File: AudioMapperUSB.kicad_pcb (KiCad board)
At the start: 2 copper layers, 100 x 100 mm, 152 parts, among them J1 USB_B, J10 Conn_01x01, J11 Conn_01x01, J12 Conn_Coaxial, J13 Conn_Coaxial, J14 Conn_Coaxial, J15 Conn_Coaxial, J16 Audio-Jack-2, J17 Audio-Jack-2, J18 Audio-Jack-2, J19 Audio-Jack-2, J2 Audio-Jack-2, J20 Audio-Jack-2, J21 Audio-Jack-2, J3 Conn_01x02, J4 Audio-Jack-2, J5 Conn_01x02, J6 Conn_01x02, J7 Conn_01x02, J8 Conn_01x01, J9 Conn_01x01, Q1 SS8550, Q2 MMBT3904, Q3 MMBT3904, U1 AMS1117-3.3, U2 PCM2900, U3 OPA2170, U4 OPA2170, U5 OPA2170, U6 OPA2170, Y1 12 MHz

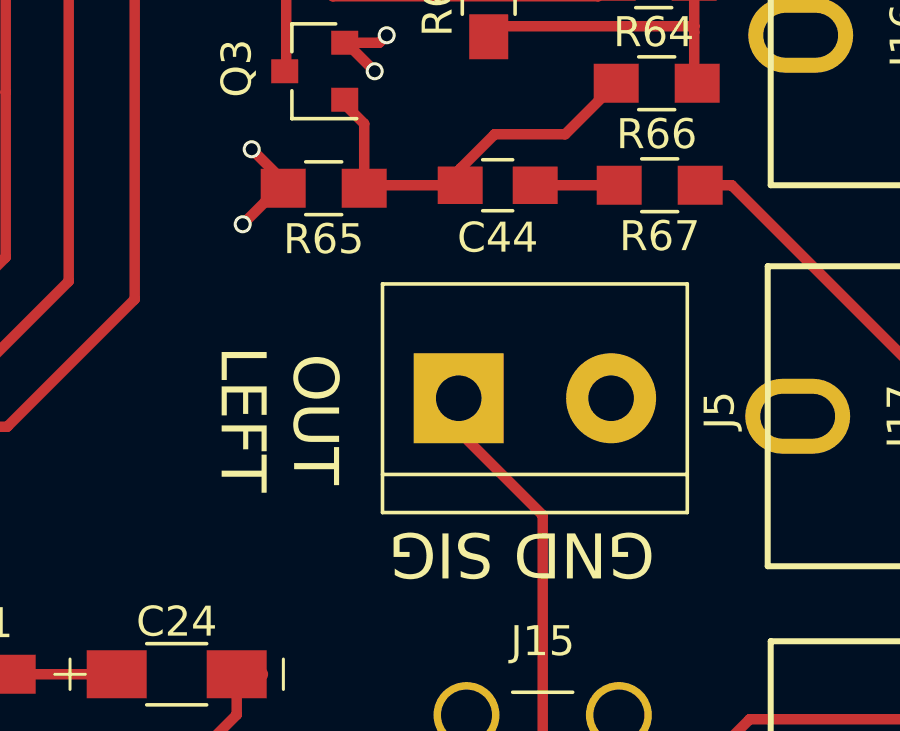
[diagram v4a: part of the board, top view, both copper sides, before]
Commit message: Added pulldown resistor to input
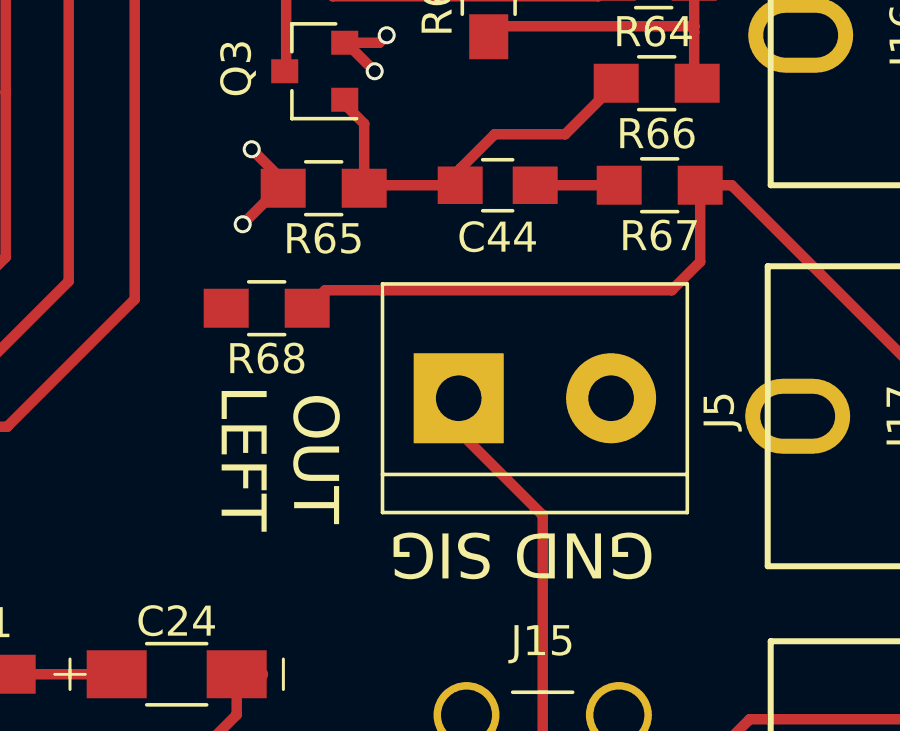
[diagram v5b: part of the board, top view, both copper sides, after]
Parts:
- added R68: 100R, Resistors_SMD:R_0805_HandSoldering, F.Cu at (100.1, 87.2)
- R67: value 100R -> 220R
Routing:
- net Net-(J17-Pad1): track 11.7 -> 28.0 mm
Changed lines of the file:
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@@
 (kicad_pcb (version 4) (host pcbnew 4.0.7)
   (general
-    (links 304)
+    (links 306)
     (no_connects 0)
     (area 28.252381 22.024999 131.74762 131.200001)
     (thickness 1.6)
     (drawings 36)
-    (tracks 1181)
+    (tracks 1185)
     (zones 0)
-    (modules 152)
+    (modules 153)
     (nets 65)
   )
@@
       (effects (font (size 1 1) (thickness 0.15)))
     )
-    (fp_text value 100R (at 0 1.75 180) (layer F.Fab)
+    (fp_text value 220R (at 0 1.75 180) (layer F.Fab)
       (effects (font (size 1 1) (thickness 0.15)))
     )
@@
     )
   )
+  (module Resistors_SMD:R_0805_HandSoldering (layer F.Cu)
+    (at 100.1 87.2 180)
+    (descr "Resistor SMD 0805, hand soldering")
+    (tags "resistor 0805")
+    (attr smd)
+    (fp_text reference R68 (at 0 -1.7 180) (layer F.SilkS)
+      (effects (font (size 1 1) (thickness 0.15)))
+    )
+    (fp_text value 100R (at 0 1.75 180) (layer F.Fab)
+      (effects (font (size 1 1) (thickness 0.15)))
+    )
+    (fp_text user %R (at 0 0 180) (layer F.Fab)
+      (effects (font (size 0.5 0.5) (thickness 0.075)))
+    )
+    (fp_line (start -1 0.62) (end -1 -0.62) (layer F.Fab) (width 0.1))
+    (fp_line (start 1 0.62) (end -1 0.62) (layer F.Fab) (width 0.1))
+    (fp_line (start 1 -0.62) (end 1 0.62) (layer F.Fab) (width 0.1))
+    (fp_line (start -1 -0.62) (end 1 -0.62) (layer F.Fab) (width 0.1))
+    (fp_line (start 0.6 0.88) (end -0.6 0.88) (layer F.SilkS) (width 0.12))
+    (fp_line (start -0.6 -0.88) (end 0.6 -0.88) (layer F.SilkS) (width 0.12))
+    (fp_line (start -2.35 -0.9) (end 2.35 -0.9) (layer F.CrtYd) (width 0.05))
+    (fp_line (start -2.35 -0.9) (end -2.35 0.9) (layer F.CrtYd) (width 0.05))
+    (fp_line (start 2.35 0.9) (end 2.35 -0.9) (layer F.CrtYd) (width 0.05))
+    (fp_line (start 2.35 0.9) (end -2.35 0.9) (layer F.CrtYd) (width 0.05))
+    (pad 1 smd rect (at -1.35 0 180) (size 1.5 1.3) (layers F.Cu F.Paste F.Mask)
+      (net 50 "Net-(J17-Pad1)"))
+    (pad 2 smd rect (at 1.35 0 180) (size 1.5 1.3) (layers F.Cu F.Paste F.Mask)
+      (net 2 GND))
+    (model ${KISYS3DMOD}/Resistors_SMD.3dshapes/R_0805.wrl
+      (at (xyz 0 0 0))
+      (scale (xyz 1 1 1))
+      (rotate (xyz 0 0 0))
+    )
+  )
   (gr_text "CHAIN IN" (at 31 106.6 270) (layer F.SilkS)
     (effects (font (size 1 1) (thickness 0.15)))
@@
     (effects (font (size 1 1) (thickness 0.15)))
   )
-  (gr_text "OUT\nLEFT" (at 100.5 90.9 270) (layer F.SilkS)
+  (gr_text "OUT\nLEFT" (at 100.5 92.2 270) (layer F.SilkS)
     (effects (font (size 1.5 1.5) (thickness 0.3)))
   )
@@
   (segment (start 127.1 67.9) (end 124.65 70.35) (width 0.35) (layer F.Cu) (net 49))
   (segment (start 124.65 70.35) (end 123.4 70.35) (width 0.35) (layer F.Cu) (net 49))
+  (segment (start 114.55 83.1) (end 114.55 85.65) (width 0.35) (layer F.Cu) (net 50))
+  (segment (start 113.6 86.6) (end 102.05 86.6) (width 0.35) (layer F.Cu) (net 50))
+  (segment (start 114.55 85.65) (end 113.6 86.6) (width 0.35) (layer F.Cu) (net 50))
+  (segment (start 102.05 86.6) (end 101.45 87.2) (width 0.35) (layer F.Cu) (net 50))
   (segment (start 122.8 90.8) (end 122.8 90.3) (width 0.35) (layer F.Cu) (net 50))
   (segment (start 122.8 90.3) (end 115.6 83.1) (width 0.35) (layer F.Cu) (net 50))

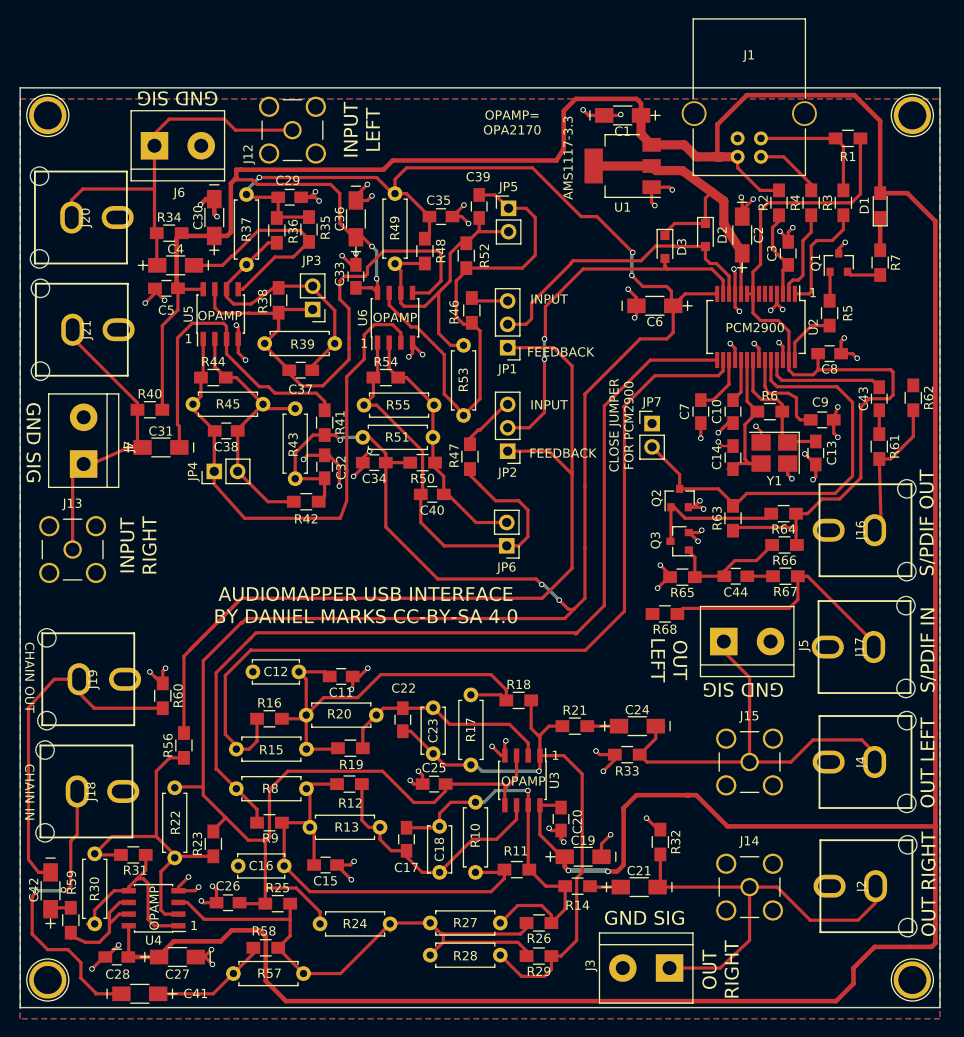
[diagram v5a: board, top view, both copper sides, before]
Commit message: Fixed backward polarity audio connectors.  Duh.
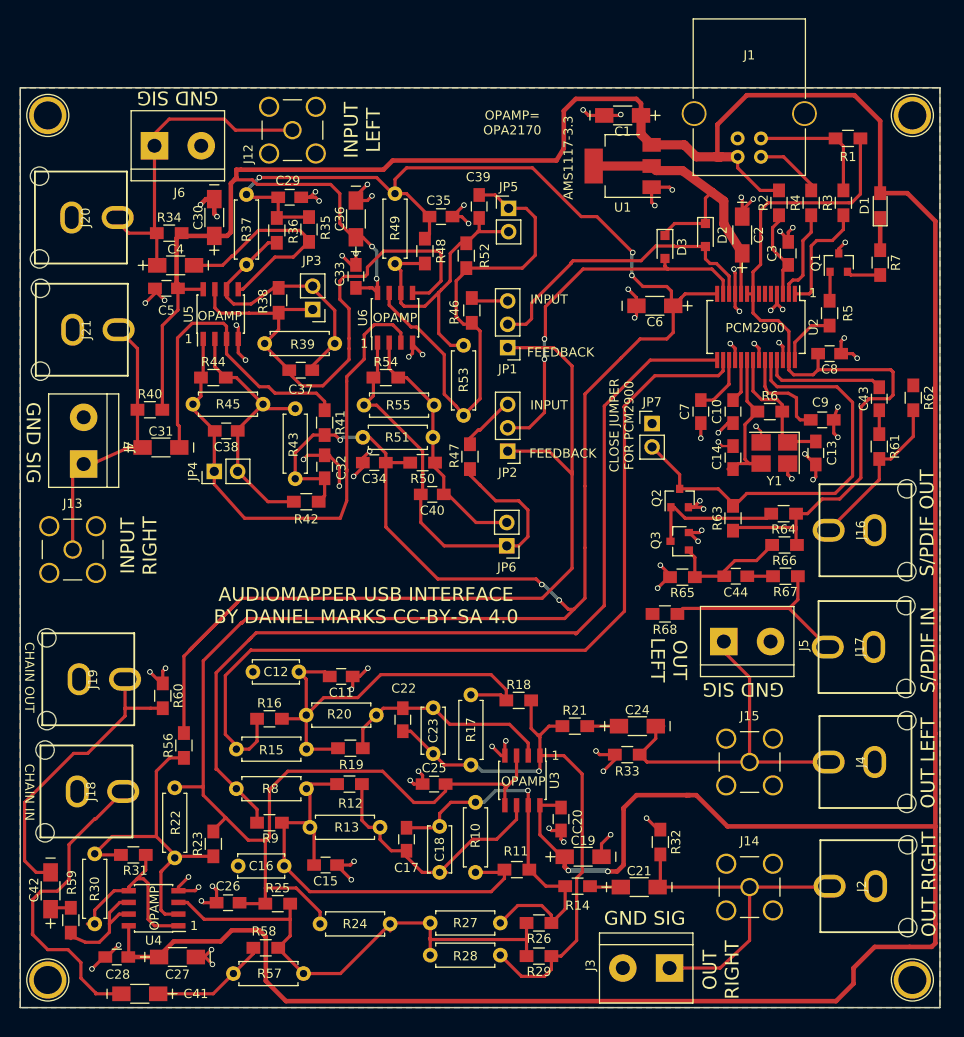
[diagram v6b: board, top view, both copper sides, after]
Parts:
- R63, R64: value 10k -> 1k
- R65: value 2k2 -> 10k
- R66: value 10k -> 100k
- R67: value 220R -> 100R
- R68: value 100R -> NC
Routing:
- net Net-(C21-Pad2): track 47.7 -> 38.7 mm
- net Net-(C24-Pad2): track 47.3 -> 39.8 mm
- net GND: track 154.9 -> 161.5 mm
- net Net-(C4-Pad1): track 42.9 -> 36.8 mm
- net Net-(R24-Pad2): track 64.0 -> 58.2 mm
- net Net-(J17-Pad1): track 28.0 -> 22.2 mm
- net Net-(C42-Pad2): track 39.4 -> 34.2 mm
- net Net-(C31-Pad1): track 32.7 -> 30.7 mm
- net Net-(J16-Pad1): track 15.6 -> 17.6 mm
- net Net-(C41-Pad2): track 33.8 -> 34.2 mm, vias 2 -> 0

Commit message: Added external power
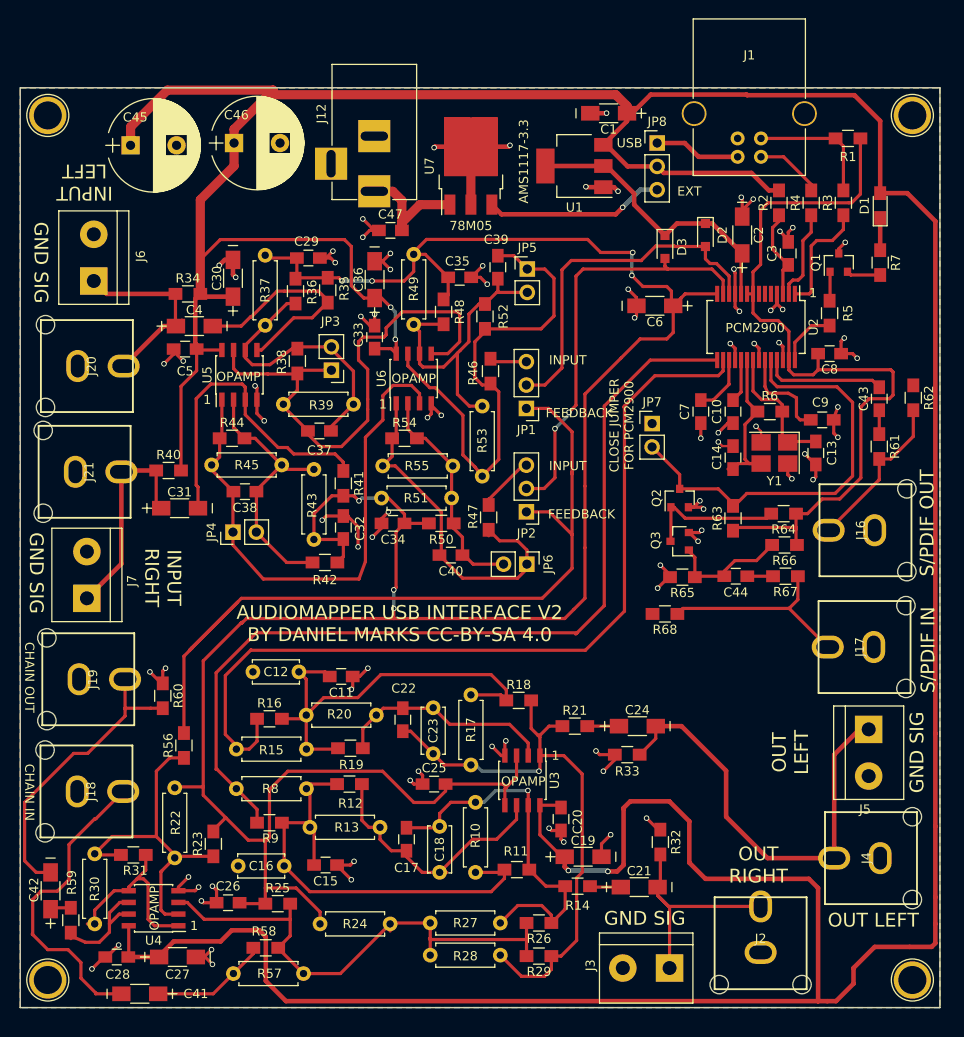
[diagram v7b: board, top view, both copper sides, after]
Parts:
- removed J13, J14, J15: Conn_Coaxial, Connectors:SMA_THT_Jack_Straight
- added C45: 1000 uF, Capacitors_THT:CP_Radial_D10.0mm_P5.00mm, F.Cu at (42.0, 36.2)
- added C46: 1000 uF, Capacitors_THT:CP_Radial_D10.0mm_P5.00mm, F.Cu at (53.2, 36.0)
- added C47: 1 uF, Capacitors_SMD:C_0805_HandSoldering, F.Cu at (70.2, 45.5)
- added JP8: Jumper_NC_Dual, Pin_Headers:Pin_Header_Straight_1x03_Pitch2.54mm, F.Cu at (99.2, 36.0)
- added U7: KA78M05_TO252, TO_SOT_Packages_SMD:TO-252-3_TabPin2, F.Cu at (79.0, 38.5)
- J12: value Conn_Coaxial -> Jack-DC; footprint Connectors:SMA_THT_Jack_Straight -> Connectors:BARREL_JACK
- moved J5 18.4 mm to (122.2, 99.8), turned to 270 degrees
- moved J20 16.2 mm to (37.2, 60.2)
- moved J6 16.1 mm to (38.0, 51.0), turned to 90 degrees
- moved J21 15.5 mm to (37.0, 71.8)
- moved J7 14.6 mm to (37.2, 85.5)
- moved J2 13.1 mm to (110.5, 123.0), turned to 180 degrees
- moved J12 11.1 mm to (68.5, 41.2), turned to 270 degrees
- moved J4 10.5 mm to (122.5, 113.8)
- moved C4 6.91 mm to (48.9, 55.9)
- moved C5 6.91 mm to (47.9, 58.4)
- moved R34 6.91 mm to (48.2, 52.4)
- moved JP5 6.91 mm to (85.1, 49.7)
- moved R46 6.91 mm to (81.1, 60.8)
- moved C29 6.91 mm to (61.3, 48.5)
- moved C31 6.91 mm to (47.3, 75.7)
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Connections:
- J1 pad 1: Net-(C1-Pad1) -> Net-(J1-Pad1)
- J12 pad 1: Net-(C4-Pad1) -> Net-(C47-Pad2)
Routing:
- net Net-(C1-Pad1): track 416.8 -> 466.7 mm
- net VCOM: track 308.3 -> 275.6 mm, vias 6 -> 7
- net Net-(JP8-Pad3): track 0.00 -> 19.5 mm, vias 0 -> 1
- net Net-(C4-Pad1): track 36.8 -> 21.7 mm
- net Net-(C47-Pad2): track 0.00 -> 13.5 mm
- net Net-(C21-Pad2): track 38.7 -> 25.3 mm
- net GND: track 161.5 -> 174.8 mm, vias 79 -> 82
- net Net-(JP1-Pad1): track 100.5 -> 89.5 mm
- net Net-(J1-Pad1): track 0.00 -> 9.37 mm
- net Net-(C24-Pad2): track 39.8 -> 49.0 mm
- net Net-(C40-Pad2): track 49.2 -> 40.4 mm
- net Net-(C31-Pad1): track 30.7 -> 23.7 mm
- net VINL: track 32.7 -> 38.7 mm
- net VINR: track 40.5 -> 46.0 mm
- net Net-(C2-Pad1): track 35.1 -> 32.0 mm
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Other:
- board text added: "78M05"
- board text added: "AUDIOMAPPER USB INTERFACE V2 BY DANIEL MARKS CC-BY-SA 4.0"
- board text added: "EXT"
- board text added: "USB"
- board text removed: "AUDIOMAPPER USB INTERFACE BY DANIEL MARKS CC-BY-SA 4.0"
- board text removed: "OPAMP= OPA2170"

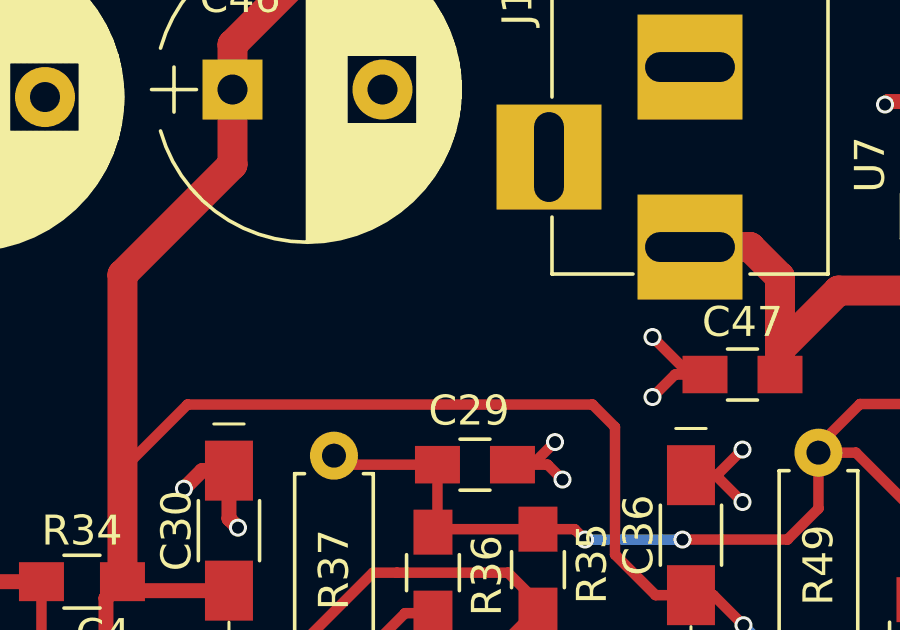
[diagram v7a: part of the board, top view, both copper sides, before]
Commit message: Added external power
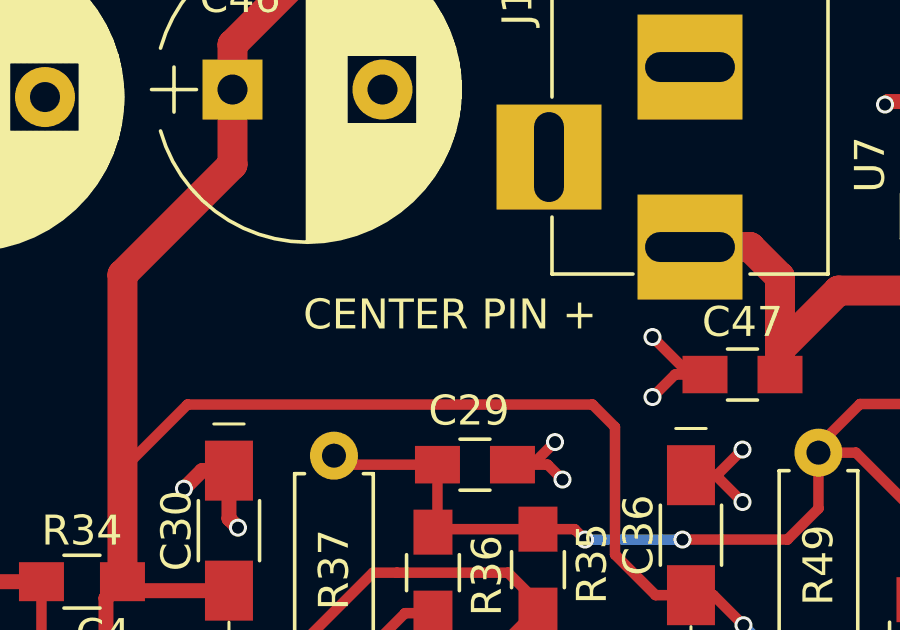
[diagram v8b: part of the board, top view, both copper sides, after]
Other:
- board text added: "CENTER PIN +"
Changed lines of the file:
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@@
     (area 29.924999 29.924999 130.075001 130.075001)
     (thickness 1.6)
-    (drawings 37)
+    (drawings 38)
     (tracks 1197)
     (zones 0)
@@
   )
   (setup
-    (last_trace_width 0.35)
+    (last_trace_width 0.25)
     (user_trace_width 0.35)
     (user_trace_width 0.5)
@@
     )
   )
+  (gr_text "CENTER PIN +" (at 60.5 43.5) (layer F.SilkS)
+    (effects (font (size 1 1) (thickness 0.15)))
+  )
   (gr_text EXT (at 102.75 41.25) (layer F.SilkS)
